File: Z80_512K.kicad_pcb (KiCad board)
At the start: 2 copper layers, 92.5 x 73.5 mm, 24 parts, among them J1 USB_B_Mini, J2 EXPANSION-BUS, SW1 ON|OFF, SW2 Z80-RESET, U1 Z84C00/PLCC, U2 74HC574, U3 512K-SRAM, U4 74HC138, U5 512K-EEPROM, U6 74HC74, U7 74HC00, Y1 20MHz-DIP14

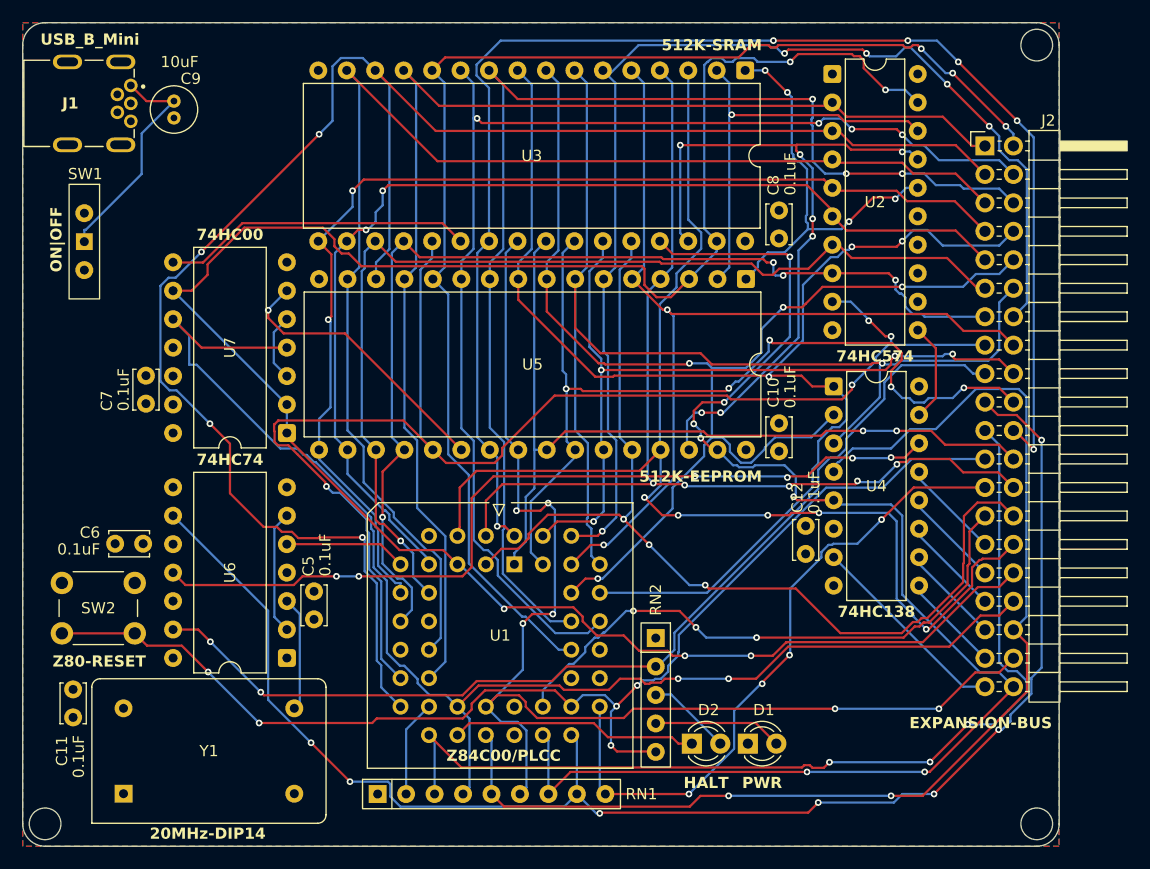
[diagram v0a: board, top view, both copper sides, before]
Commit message: Refine Expansion-Bus: remove all EXs & add VCC/GND rails + Diode/USB.
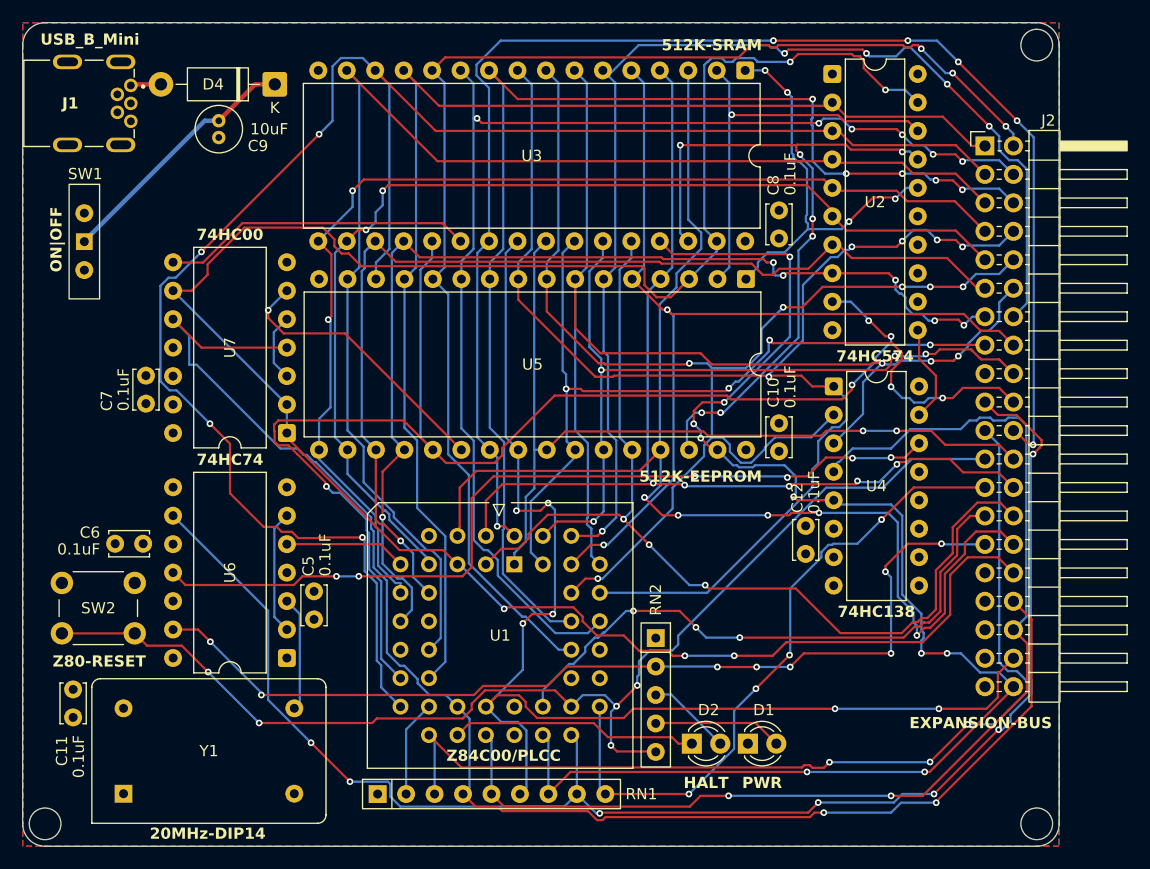
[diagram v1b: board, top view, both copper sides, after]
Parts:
- added D4: D_Schottky, Diode_THT:D_DO-41_SOD81_P10.16mm_Horizontal, F.Cu at (125.0, 36.5)
- moved C9 4.37 mm to (120.0, 41.2)
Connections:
- C9 pad 2: Net-(J1-VBUS) -> Net-(D4-K)
- J1 pad 1: Net-(J1-VBUS) -> Net-(D4-A)
- J2 pad 17: /WAIT_RE -> GND
- J2 pad 29: /EX0 -> /WAIT_RE
- J2 pad 31: /EX1 -> GND
- J2 pad 33: /EX2 -> VCC
- J2 pad 35: /EX3 -> GND
- J2 pad 37: /EX4 -> VCC
- J2 pad 39: /EX5 -> GND
- SW1 pad 1: Net-(J1-VBUS) -> Net-(D4-K)
- U4 pad 10: /EX3 -> unconnected-(U4-~{Y5}-Pad10)
- U4 pad 11: /EX2 -> unconnected-(U4-~{Y4}-Pad11)
- U4 pad 12: /EX1 -> unconnected-(U4-~{Y3}-Pad12)
- U4 pad 13: /EX0 -> unconnected-(U4-~{Y2}-Pad13)
- U4 pad 7: /EX5 -> unconnected-(U4-~{Y7}-Pad7)
- U4 pad 9: /EX4 -> unconnected-(U4-~{Y6}-Pad9)
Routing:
- net Net-(D4-K): track 0.00 -> 22.8 mm
- net Net-(J1-VBUS): track 20.4 -> 0.00 mm
- net /EX5: track 18.3 -> 0.00 mm
- net /MREQ: track 121.6 -> 133.4 mm
- net /EX4: track 8.92 -> 0.00 mm
- net /EX2: track 8.92 -> 0.00 mm
- net /EX0: track 8.92 -> 0.00 mm
- net /EX3: track 8.92 -> 0.00 mm
- net /EX1: track 8.92 -> 0.00 mm
- net /WAIT_RE: track 91.0 -> 85.7 mm, vias 2 -> 8
- net /A14: track 110.8 -> 115.4 mm
- net /IORQ: track 106.1 -> 102.7 mm
- net /MEM_A15: track 189.9 -> 193.1 mm
- net Net-(D4-A): track 0.00 -> 2.73 mm
- net /WR: track 127.1 -> 129.3 mm, vias 7 -> 9
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
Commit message: Rev1.1: fixed 74HC00/74 footprint, schematic(CE,Bus,574..), layout.
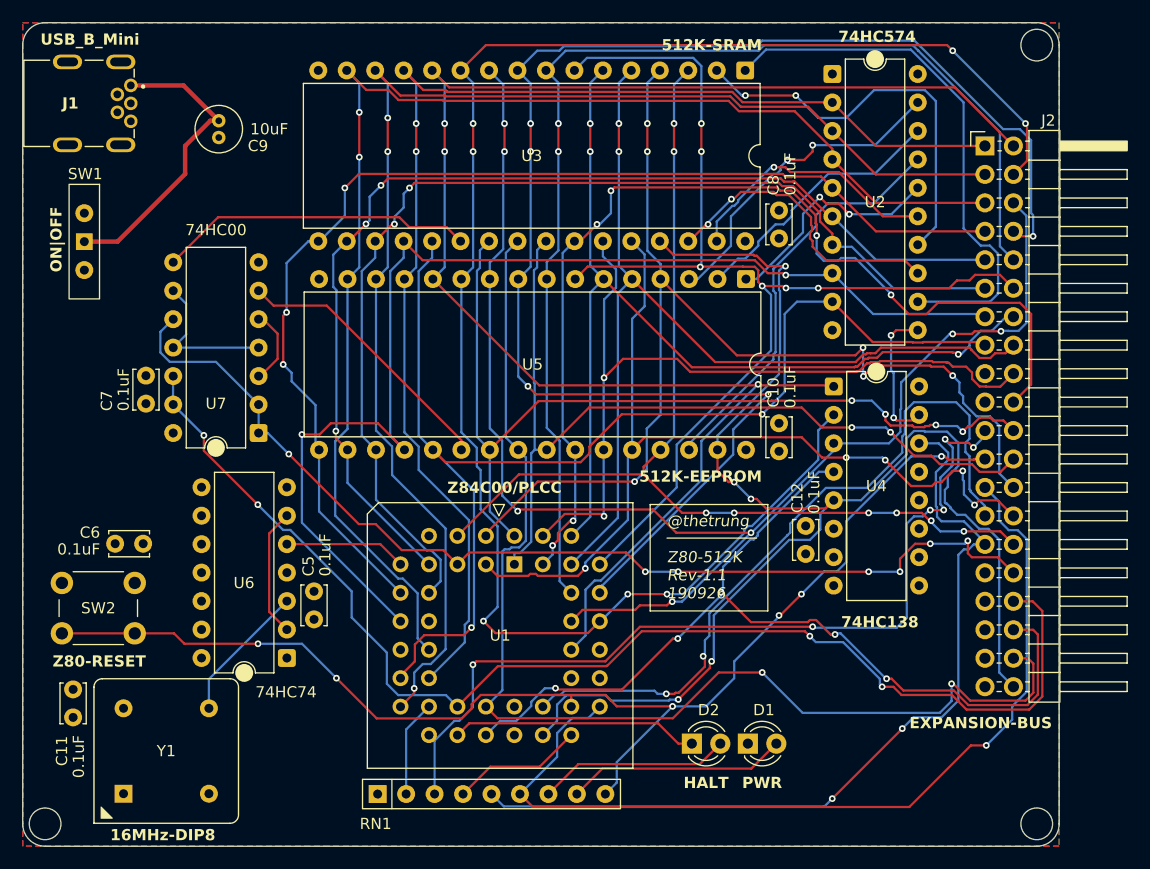
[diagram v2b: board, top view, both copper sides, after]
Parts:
- removed D4: D_Schottky, Diode_THT:D_DO-41_SOD81_P10.16mm_Horizontal
- removed RN2: RN_10K, Resistor_THT:R_Array_SIP5
- U6, U7: footprint Package_DIP:DIP-14_W10.16mm -> Package_DIP:DIP-14_W7.62mm
- Y1: value 20MHz-DIP14 -> 16MHz-DIP8; footprint Oscillator:Oscillator_DIP-14 -> Oscillator:Oscillator_DIP-8
- moved U7 2.52 mm to (123.6, 67.6)
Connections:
- net /PORT_38 renamed /PORT_00
- net Net-(U7-Pad3) renamed /A15_INVERT
- C9 pad 2: Net-(D4-K) -> Net-(J1-VBUS)
- J1 pad 1: Net-(D4-A) -> Net-(J1-VBUS)
- J2 pad 19: /WAIT -> VCC
- J2 pad 29: /WAIT_RE -> /PORT_01
- J2 pad 32: /MEM_A15 -> /A15
- RN1 pad 4: /MREQ -> /WAIT
- RN1 pad 5: /IORQ -> /PORT_01
- RN1 pad 6: /RD -> /BUSREQ
- RN1 pad 7: /WR -> Net-(D2-A)
- RN1 pad 8: /WAIT -> Net-(D1-A)
- RN1 pad 9: /BUSREQ -> /RESET
- SW1 pad 1: Net-(D4-K) -> Net-(J1-VBUS)
- U1 pad 5: /MEM_A15 -> /A15
- U2 pad 12: unconnected-(U2-Q7-Pad12) -> /RAM_A18
- U2 pad 13: unconnected-(U2-Q6-Pad13) -> /RAM_A17
- U2 pad 14: unconnected-(U2-Q5-Pad14) -> /RAM_A16
- U2 pad 15: unconnected-(U2-Q4-Pad15) -> /RAM_A15
- U2 pad 16: /MEM_A18 -> /ROM_A18
- U2 pad 17: /MEM_A17 -> /ROM_A17
- U2 pad 18: /MEM_A16 -> /ROM_A16
- U2 pad 19: /MEM_A15 -> /ROM_A15
- U3 pad 1: /MEM_A18 -> /RAM_A18
- U3 pad 2: /MEM_A16 -> /RAM_A16
- U3 pad 30: /MEM_A17 -> /RAM_A17
- U3 pad 31: /MEM_A15 -> /RAM_A15
- U4 pad 1: /A3 -> /A0
- U4 pad 14: /PORT_39 -> /PORT_01
- U4 pad 2: /A4 -> /A1
- U4 pad 3: /A5 -> /A2
- U5 pad 1: /MEM_A18 -> /ROM_A18
- U5 pad 2: /MEM_A16 -> /ROM_A16
- U5 pad 3: /MEM_A15 -> /ROM_A15
- U5 pad 30: /MEM_A17 -> /ROM_A17
- U6 pad 10: VCC -> unconnected-(U6B-~{S}-Pad10)
- U6 pad 11: /PORT_39 -> unconnected-(U6B-C-Pad11)
- U6 pad 12: GND -> unconnected-(U6B-D-Pad12)
- U6 pad 13: /WAIT_RE -> unconnected-(U6B-~{R}-Pad13)
- U6 pad 3: /20CLK -> /16CLK
- U6 pad 9: /WAIT -> unconnected-(U6B-Q-Pad9)
- U7 pad 1: /MEM_A15 -> /A15
- U7 pad 10: /MREQ -> /A15
- U7 pad 11: unconnected-(U7-Pad11) -> /MREQ_INVERT
- U7 pad 12: VCC -> /MREQ
- U7 pad 13: VCC -> /MREQ
- U7 pad 2: /MEM_A15 -> /A15
- U7 pad 4: /MREQ -> /MREQ_INVERT
- U7 pad 9: /MEM_A15 -> /MREQ_INVERT
- Y1 pad 8: /20CLK -> VCC
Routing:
- net /MEM_A15: track 193.1 -> 0.00 mm, vias 5 -> 0
- net /WAIT: track 133.6 -> 11.8 mm, vias 7 -> 0
- net /A15: track 0.00 -> 93.7 mm, vias 0 -> 7
- net /WAIT_RE: track 85.7 -> 0.00 mm, vias 8 -> 0
- net /PORT_01: track 0.00 -> 76.4 mm, vias 0 -> 2
- net /PORT_39: track 76.0 -> 0.00 mm, vias 6 -> 0
- net /MEM_A17: track 64.6 -> 0.00 mm, vias 7 -> 0
- net /A10: track 128.7 -> 79.5 mm, vias 6 -> 4
- net /RAM_A18: track 0.00 -> 48.5 mm
- net /A1: track 109.9 -> 152.7 mm, vias 6 -> 7
- net /D1: track 160.3 -> 120.6 mm, vias 4 -> 3
- net /MEM_A16: track 36.9 -> 0.00 mm, vias 1 -> 0
- net /ROM_A17: track 0.00 -> 36.9 mm
- net /MEM_A18: track 36.8 -> 0.00 mm, vias 4 -> 0
- net /RAM_A16: track 0.00 -> 36.2 mm, vias 0 -> 2
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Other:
- board text added: "@thetrung Z80-512K Rev-1.1 190926"

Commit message: Add 1xCap + adjust closer->74HC74.
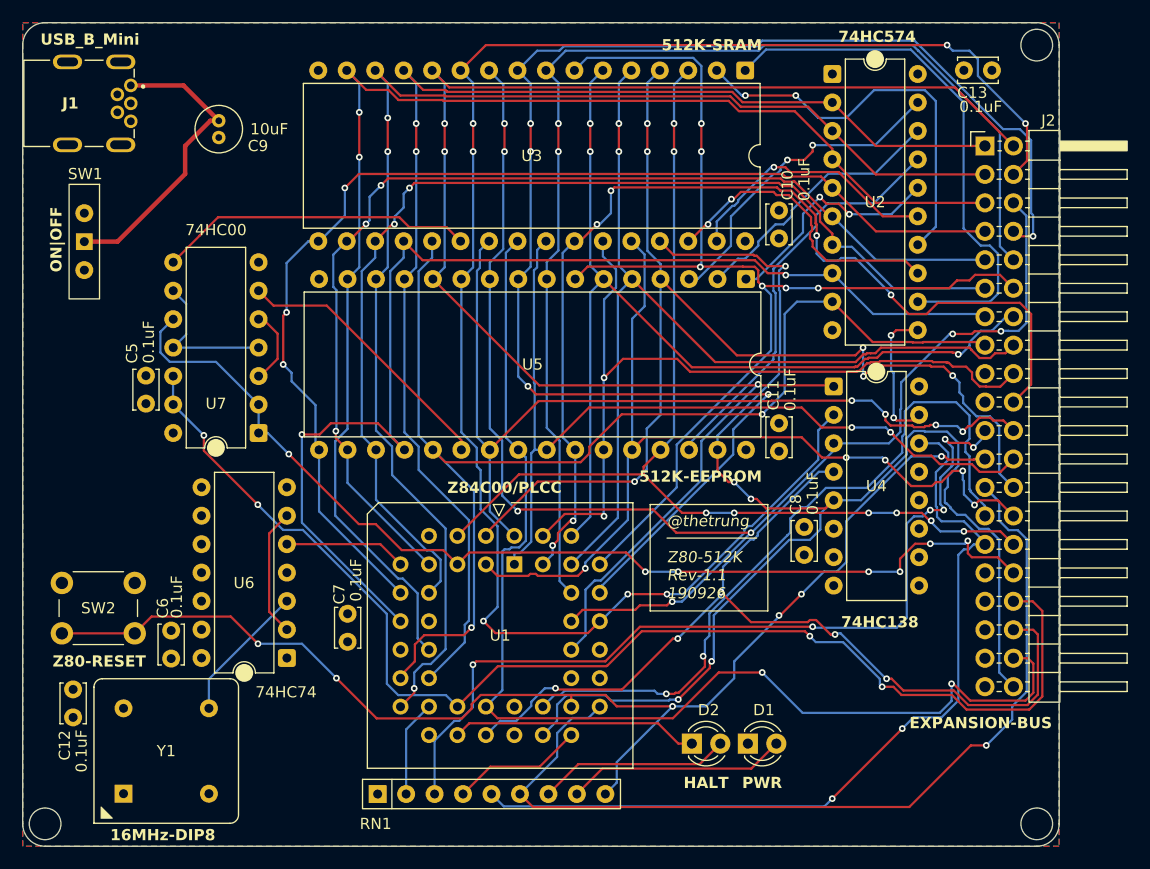
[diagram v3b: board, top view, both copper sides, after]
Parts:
- added C13: 0.1uF, Capacitor_THT:C_Disc_D3.4mm_W2.1mm_P2.50mm, F.Cu at (189.0, 35.2)
- moved C11 68.2 mm to (170.0, 66.8), turned to -90 degrees
- moved C12 67.0 mm to (107.0, 93.0)
- moved C8 30.8 mm to (172.2, 78.5), turned to 90 degrees
- moved C7 26.0 mm to (131.5, 83.8), turned to -90 degrees
- moved C5 22.5 mm to (113.5, 65.0), turned to 90 degrees
- moved C10 19.0 mm to (170.0, 47.8)
- moved C6 9.22 mm to (115.8, 85.2), turned to -90 degrees
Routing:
- net /RESET: track 110.9 -> 112.1 mm
- net /A1: track 152.7 -> 153.6 mm
- net /MREQ: track 112.1 -> 112.8 mm

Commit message: Rev1.2: Fix 74HC574/74 for Bank0.
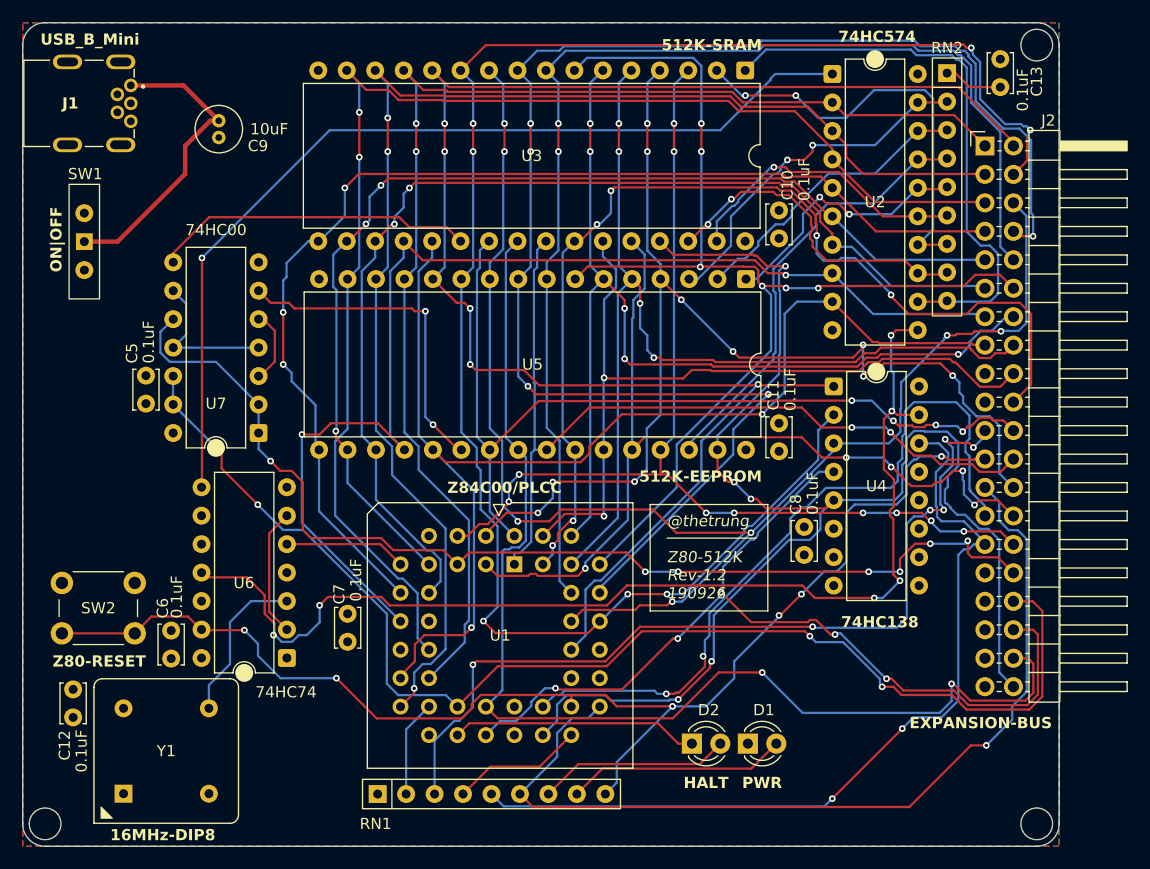
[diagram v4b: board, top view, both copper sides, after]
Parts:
- added RN2: RN_10K, Resistor_THT:R_Array_SIP9, F.Cu at (185.0, 35.5)
- moved C13 1.68 mm to (189.8, 36.8), turned to 90 degrees
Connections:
- U2 pad 1: GND -> /574_OE
- U6 pad 10: unconnected-(U6B-~{S}-Pad10) -> VCC
- U6 pad 11: unconnected-(U6B-C-Pad11) -> /PORT_00
- U6 pad 12: unconnected-(U6B-D-Pad12) -> VCC
- U6 pad 13: unconnected-(U6B-~{R}-Pad13) -> /RESET
- U6 pad 8: unconnected-(U6B-~{Q}-Pad8) -> /574_OE
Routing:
- net /PORT_00: track 12.6 -> 99.8 mm, vias 2 -> 6
- net /574_OE: track 0.00 -> 83.6 mm, vias 0 -> 1
- net GND: track 0.00 -> 5.27 mm
- net /ROM_CE: track 24.5 -> 29.5 mm, vias 0 -> 2
- net /A15: track 93.7 -> 97.0 mm
- net /A0: track 144.9 -> 148.1 mm, vias 3 -> 5
- net /RAM_A17: track 27.0 -> 30.1 mm
- net /A7: track 85.8 -> 88.8 mm, vias 2 -> 4
- net /A6: track 85.8 -> 88.6 mm, vias 3 -> 5
- net /ROM_A18: track 20.9 -> 23.8 mm
- net /ROM_A17: track 36.9 -> 39.6 mm
- net /RAM_A15: track 23.6 -> 26.3 mm
- net /ROM_A16: track 23.9 -> 26.5 mm
- net /ROM_A15: track 29.0 -> 31.6 mm
- net /RESET: track 112.1 -> 114.6 mm
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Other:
- board text added: "@thetrung Z80-512K Rev-1.2 190926"
- board text removed: "@thetrung Z80-512K Rev-1.1 190926"

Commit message: Rev1.2.1: refine RESET circuit.
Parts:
- added C14: 10uF, Capacitor_THT:C_Radial_D4.0mm_H5.0mm_P1.50mm, F.Cu at (108.5, 77.0)
- added D3: 1N4148, Diode_THT:D_DO-35_SOD27_P7.62mm_Horizontal, F.Cu at (106.5, 65.4)
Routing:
- net /RESET: track 114.6 -> 129.5 mm
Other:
- board text added: "@thetrung Z80-512K Rev-1.2.1 190926"
- board text removed: "@thetrung Z80-512K Rev-1.2 190926"
